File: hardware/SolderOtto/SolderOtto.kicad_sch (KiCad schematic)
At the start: 0 parts

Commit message: fix electrical findings
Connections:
- no-connect marks 4 -> 49
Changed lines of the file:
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@@
 	(paper "A4")
 	(no_connect
+		(at 177.8 55.88)
+	)
+	(no_connect
+		(at 177.8 86.36)
+	)
+	(no_connect
+		(at 177.8 147.32)
+	)
+	(no_connect
+		(at 177.8 72.39)
+	)
+	(no_connect
+		(at 76.2 152.4)
+	)
+	(no_connect
+		(at 76.2 140.97)
+	)
+	(no_connect
+		(at 76.2 132.08)
+	)
+	(no_connect
+		(at 177.8 81.28)
+	)
+	(no_connect
+		(at 177.8 78.74)
+	)
+	(no_connect
+		(at 177.8 129.54)
+	)
+	(no_connect
 		(at 152.4 38.1)
+	)
+	(no_connect
+		(at 177.8 74.93)
+	)
+	(no_connect
+		(at 177.8 69.85)
 	)
 	(no_connect
@@
 	)
 	(no_connect
+		(at 76.2 121.92)
+	)
+	(no_connect
+		(at 76.2 127)
+	)
+	(no_connect
+		(at 76.2 154.94)
+	)
+	(no_connect
+		(at 177.8 95.25)
+	)
+	(no_connect
+		(at 76.2 118.11)
+	)
+	(no_connect
+		(at 177.8 83.82)
+	)
+	(no_connect
+		(at 177.8 115.57)
+	)
+	(no_connect
+		(at 177.8 60.96)
+	)
+	(no_connect
+		(at 76.2 149.86)
+	)
+	(no_connect
+		(at 177.8 121.92)
+	)
+	(no_connect
+		(at 76.2 115.57)
+	)
+	(no_connect
+		(at 177.8 127)
+	)
+	(no_connect
+		(at 177.8 140.97)
+	)
+	(no_connect
+		(at 177.8 154.94)
+	)
+	(no_connect
+		(at 177.8 138.43)
+	)
+	(no_connect
+		(at 177.8 143.51)
+	)
+	(no_connect
 		(at 142.24 38.1)
+	)
+	(no_connect
+		(at 76.2 143.51)
+	)
+	(no_connect
+		(at 177.8 118.11)
+	)
+	(no_connect
+		(at 177.8 97.79)
+	)
+	(no_connect
+		(at 177.8 64.77)
 	)
 	(no_connect
 		(at 154.94 38.1)
 	)
+	(no_connect
+		(at 177.8 149.86)
+	)
+	(no_connect
+		(at 177.8 135.89)
+	)
+	(no_connect
+		(at 177.8 152.4)
+	)
+	(no_connect
+		(at 76.2 113.03)
+	)
+	(no_connect
+		(at 177.8 113.03)
+	)
+	(no_connect
+		(at 177.8 132.08)
+	)
+	(no_connect
+		(at 177.8 58.42)
+	)
+	(no_connect
+		(at 76.2 138.43)
+	)
+	(no_connect
+		(at 76.2 135.89)
+	)
+	(no_connect
+		(at 76.2 147.32)
+	)
+	(no_connect
+		(at 177.8 90.17)
+	)
+	(no_connect
+		(at 76.2 129.54)
+	)
+	(no_connect
+		(at 177.8 92.71)
+	)
 	(wire

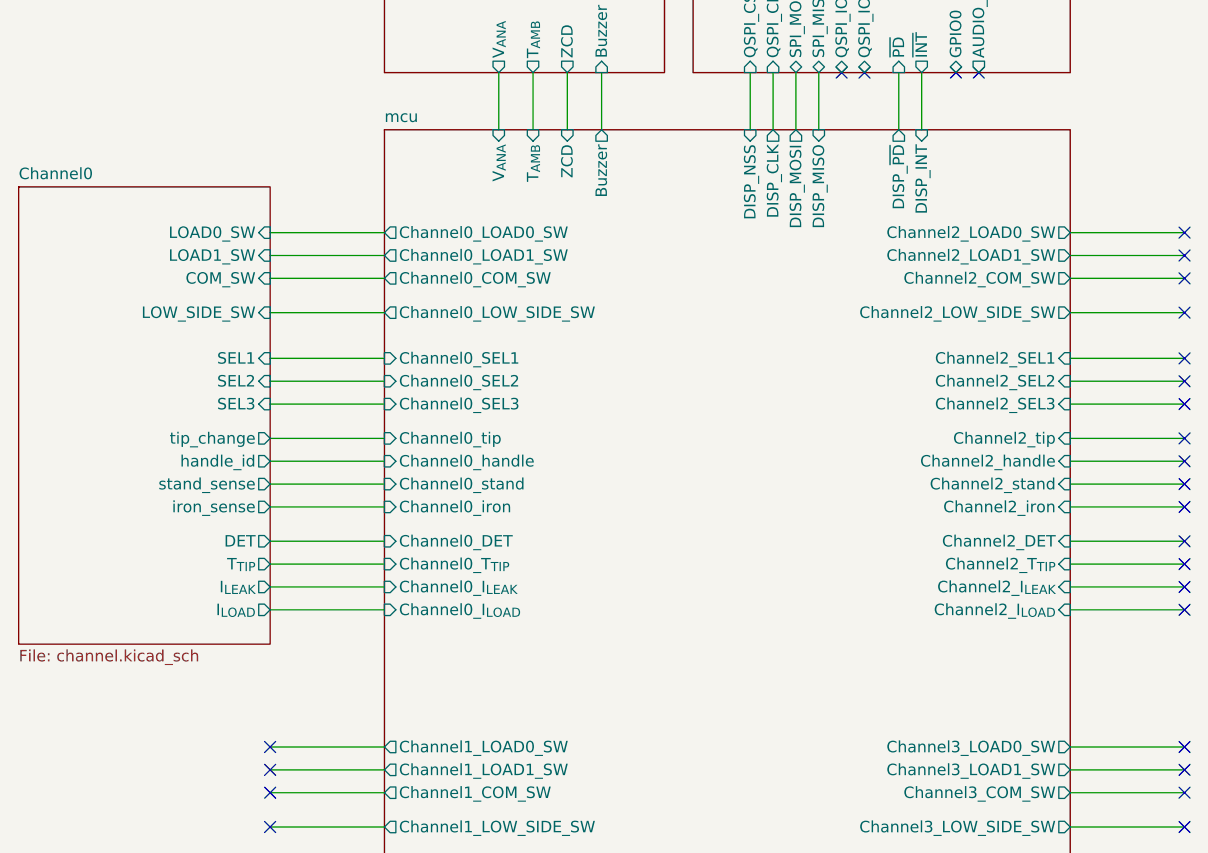
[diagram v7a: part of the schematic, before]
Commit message: remove low side switching ic
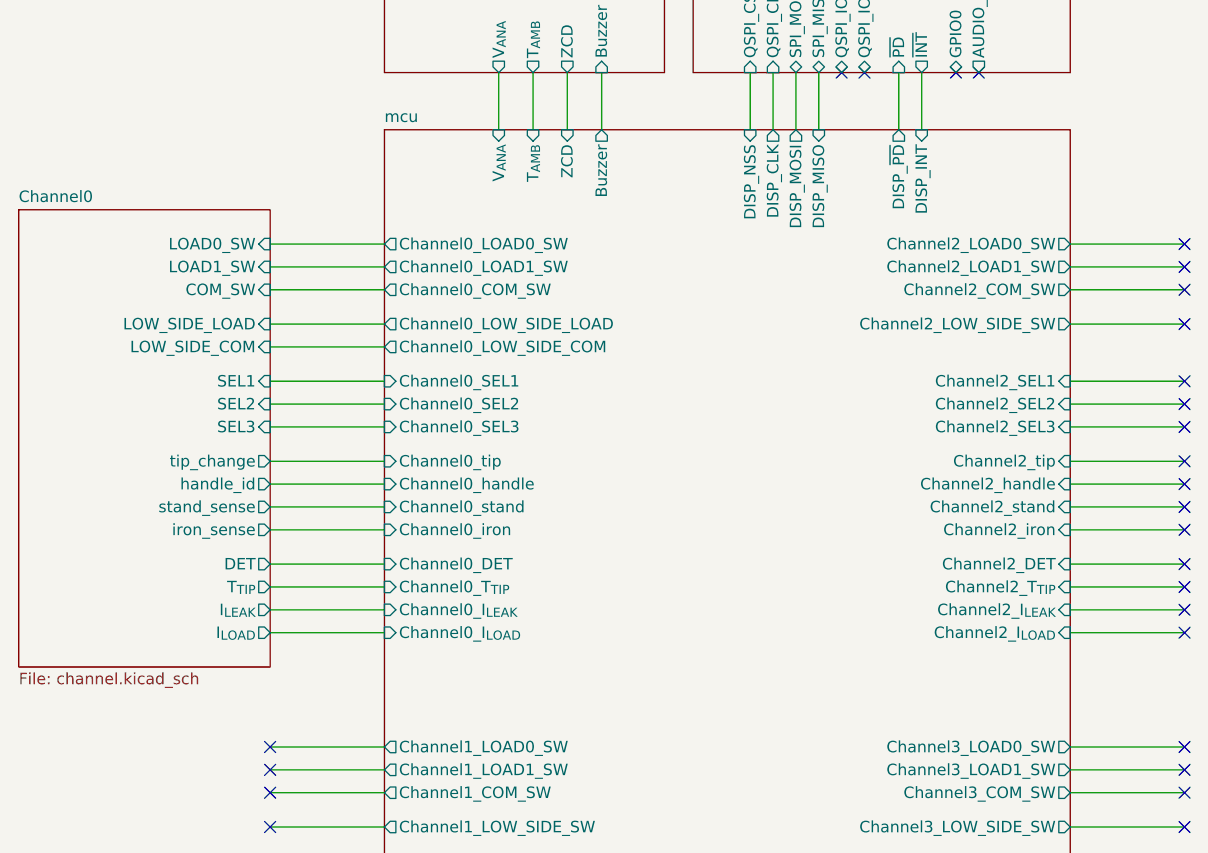
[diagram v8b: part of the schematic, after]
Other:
- sheet Channel0 ports: added LOW_SIDE_COM, LOW_SIDE_LOAD; removed LOW_SIDE_SW
- sheet mcu ports: added Channel0_LOW_SIDE_COM, Channel0_LOW_SIDE_LOAD; removed Channel0_LOW_SIDE_SW
